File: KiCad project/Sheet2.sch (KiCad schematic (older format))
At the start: 7 parts, among them U1 EFM32GG332, X1 SMD_32.768kHz_CRYSTAL_OSC, X2 SMD_48MHZ_CRYSTAL_OSC

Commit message: IC packages, bugfixes
drawings for IC packages, associations, schematic fixes
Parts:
- U1: footprint (none) -> Housings_QFP:TQFP-64_10x10mm_Pitch0.5mm
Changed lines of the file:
@@
 $Descr A4 11693 8268
 encoding utf-8
-Sheet 3 7
+Sheet 3 10
 Title "uC part A"
 Date "14 March 2015"
@@
 F 0 "U1" H 7450 850 60  0000 C CNN
 F 1 "EFM32GG332" H 8850 850 60  0000 C CNN
-F 2 "" H 8850 850 60  0000 C CNN
+F 2 "Housings_QFP:TQFP-64_10x10mm_Pitch0.5mm" H 8850 850 60  0001 C CNN
 F 3 "" H 8850 850 60  0000 C CNN
 	1    7350 900
@@
 F 0 "X2" H 4900 3290 50  0000 C CNN
 F 1 "SMD_48MHZ_CRYSTAL_OSC" H 4930 3090 50  0000 L CNN
-F 2 "" H 4900 3200 60  0000 C CNN
+F 2 "" H 4900 3200 60  0001 C CNN
 F 3 "" H 4900 3200 60  0000 C CNN
 	1    4900 3200
@@
 F 0 "C17" H 4750 2950 50  0000 L CNN
 F 1 "C" H 4750 2750 50  0000 L CNN
-F 2 "" H 4738 2700 30  0000 C CNN
+F 2 "" H 4738 2700 30  0001 C CNN
 F 3 "" H 4700 2850 60  0000 C CNN
 	1    4700 2850
@@
 F 0 "C18" H 5150 2950 50  0000 L CNN
 F 1 "C" H 5150 2750 50  0000 L CNN
-F 2 "" H 5138 2700 30  0000 C CNN
+F 2 "" H 5138 2700 30  0001 C CNN
 F 3 "" H 5100 2850 60  0000 C CNN
 	1    5100 2850
@@
 	4700 3200 4700 3050
 $Comp
-L GND #PWR14
+L GND #PWR017
 U 1 1 5504D536
 P 4900 2500
-F 0 "#PWR14" H 4900 2250 60  0001 C CNN
+F 0 "#PWR017" H 4900 2250 60  0001 C CNN
 F 1 "GND" H 4900 2350 60  0000 C CNN
 F 2 "" H 4900 2500 60  0000 C CNN
@@
 F 0 "X1" H 5550 2590 50  0000 C CNN
 F 1 "SMD_32.768kHz_CRYSTAL_OSC" H 5580 2390 50  0000 L CNN
-F 2 "" H 5550 2500 60  0000 C CNN
+F 2 "" H 5550 2500 60  0001 C CNN
 F 3 "" H 5550 2500 60  0000 C CNN
 	1    5550 2500
@@
 F 0 "C16" H 5800 2250 50  0000 L CNN
 F 1 "C" H 5800 2050 50  0000 L CNN
-F 2 "" H 5788 2000 30  0000 C CNN
+F 2 "" H 5788 2000 30  0001 C CNN
 F 3 "" H 5750 2150 60  0000 C CNN
 	1    5750 2150
@@
 F 0 "C15" H 5400 2250 50  0000 L CNN
 F 1 "C" H 5400 2050 50  0000 L CNN
-F 2 "" H 5388 2000 30  0000 C CNN
+F 2 "" H 5388 2000 30  0001 C CNN
 F 3 "" H 5350 2150 60  0000 C CNN
 	1    5350 2150
@@
 Connection ~ 5350 2500
 $Comp
-L GND #PWR16
+L GND #PWR018
 U 1 1 5504D88A
 P 4900 3300
-F 0 "#PWR16" H 4900 3050 60  0001 C CNN
+F 0 "#PWR018" H 4900 3050 60  0001 C CNN
 F 1 "GND" H 4900 3150 60  0000 C CNN
 F 2 "" H 4900 3300 60  0000 C CNN
@@
 $EndComp
 $Comp
-L GND #PWR15
+L GND #PWR019
 U 1 1 5504D89E
 P 5550 2600
-F 0 "#PWR15" H 5550 2350 60  0001 C CNN
+F 0 "#PWR019" H 5550 2350 60  0001 C CNN
 F 1 "GND" H 5550 2450 60  0000 C CNN
 F 2 "" H 5550 2600 60  0000 C CNN

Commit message: New packages, PCB
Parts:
- removed X1: SMD_32.768kHz_CRYSTAL_OSC, symbol CRYSTAL_SMD
- added X1: 32.768kHz SMD Crystal, Anastasia:1.6x1.0CRYSTAL, symbol CRYSTAL
- C16: renamed from C15; footprint (none) -> Capacitors_SMD:C_0603
- C17: renamed from C16; footprint (none) -> Capacitors_SMD:C_0603
- C18: renamed from C17; footprint (none) -> Capacitors_SMD:C_0603
- C19: renamed from C18; footprint (none) -> Capacitors_SMD:C_0603
- X2: footprint (none) -> Anastasia:2x1.6
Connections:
- wire segments 25 -> 26
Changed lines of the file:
@@
 F 0 "X2" H 4900 3290 50  0000 C CNN
 F 1 "SMD_48MHZ_CRYSTAL_OSC" H 4930 3090 50  0000 L CNN
-F 2 "" H 4900 3200 60  0001 C CNN
+F 2 "Anastasia:2x1.6" H 4900 3200 60  0001 C CNN
 F 3 "" H 4900 3200 60  0000 C CNN
 	1    4900 3200
@@
 $EndComp
 $Comp
-L C C17
+L C C18
 U 1 1 5504D3F7
 P 4700 2850
-F 0 "C17" H 4750 2950 50  0000 L CNN
+F 0 "C18" H 4750 2950 50  0000 L CNN
 F 1 "C" H 4750 2750 50  0000 L CNN
-F 2 "" H 4738 2700 30  0001 C CNN
+F 2 "Capacitors_SMD:C_0603" H 4738 2700 30  0001 C CNN
 F 3 "" H 4700 2850 60  0000 C CNN
 	1    4700 2850
@@
 $EndComp
 $Comp
-L C C18
+L C C19
 U 1 1 5504D470
 P 5100 2850
-F 0 "C18" H 5150 2950 50  0000 L CNN
+F 0 "C19" H 5150 2950 50  0000 L CNN
 F 1 "C" H 5150 2750 50  0000 L CNN
-F 2 "" H 5138 2700 30  0001 C CNN
+F 2 "Capacitors_SMD:C_0603" H 5138 2700 30  0001 C CNN
 F 3 "" H 5100 2850 60  0000 C CNN
 	1    5100 2850
@@
 High Frequency \nCrystal Oscillator
 $Comp
-L CRYSTAL_SMD X1
-U 1 1 5504D70C
-P 5550 2500
-F 0 "X1" H 5550 2590 50  0000 C CNN
-F 1 "SMD_32.768kHz_CRYSTAL_OSC" H 5580 2390 50  0000 L CNN
-F 2 "" H 5550 2500 60  0001 C CNN
-F 3 "" H 5550 2500 60  0000 C CNN
-	1    5550 2500
-	1    0    0    -1
-$EndComp
-$Comp
-L C C16
+L C C17
 U 1 1 5504D74C
 P 5750 2150
-F 0 "C16" H 5800 2250 50  0000 L CNN
+F 0 "C17" H 5800 2250 50  0000 L CNN
 F 1 "C" H 5800 2050 50  0000 L CNN
-F 2 "" H 5788 2000 30  0001 C CNN
+F 2 "Capacitors_SMD:C_0603" H 5788 2000 30  0001 C CNN
 F 3 "" H 5750 2150 60  0000 C CNN
 	1    5750 2150
@@
 $EndComp
 $Comp
-L C C15
+L C C16
 U 1 1 5504D769
 P 5350 2150
-F 0 "C15" H 5400 2250 50  0000 L CNN
+F 0 "C16" H 5400 2250 50  0000 L CNN
 F 1 "C" H 5400 2050 50  0000 L CNN
-F 2 "" H 5388 2000 30  0001 C CNN
+F 2 "Capacitors_SMD:C_0603" H 5388 2000 30  0001 C CNN
 F 3 "" H 5350 2150 60  0000 C CNN
 	1    5350 2150
@@
 	1    0    0    -1
 $EndComp
+Text Notes 5950 2200 0    60   ~ 0
+Low Frequency\nReal-Time Clock \nCrystal Oscillator\n
 $Comp
-L GND #PWR019
-U 1 1 5504D89E
-P 5550 2600
-F 0 "#PWR019" H 5550 2350 60  0001 C CNN
-F 1 "GND" H 5550 2450 60  0000 C CNN
-F 2 "" H 5550 2600 60  0000 C CNN
-F 3 "" H 5550 2600 60  0000 C CNN
-	1    5550 2600
+L CRYSTAL X1
+U 1 1 550DBF8D
+P 5650 2700
+F 0 "X1" H 5650 2850 50  0000 C CNN
+F 1 "32.768kHz SMD Crystal" H 5650 2550 50  0000 C CNN
+F 2 "Anastasia:1.6x1.0CRYSTAL" H 5650 2700 60  0001 C CNN
+F 3 "" H 5650 2700 60  0000 C CNN
+	1    5650 2700
 	1    0    0    -1
 $EndComp
-Text Notes 5950 2200 0    60   ~ 0
-Low Frequency\nReal-Time Clock \nCrystal Oscillator\n
+Wire Wire Line
+	5950 2700 5950 2500
+Connection ~ 5950 2500
 $EndSCHEMATC

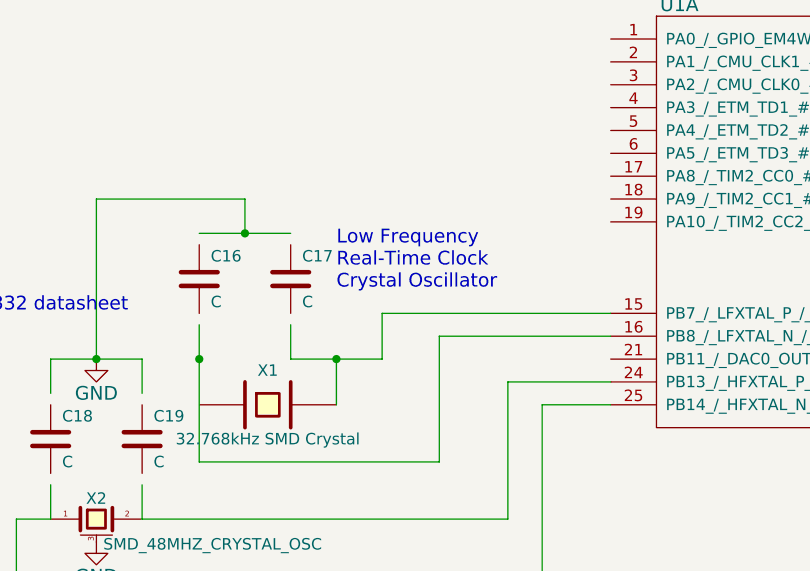
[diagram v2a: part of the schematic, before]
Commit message: Schematics, PCB design
New schematics for the pulse oximeter, PCB layout design
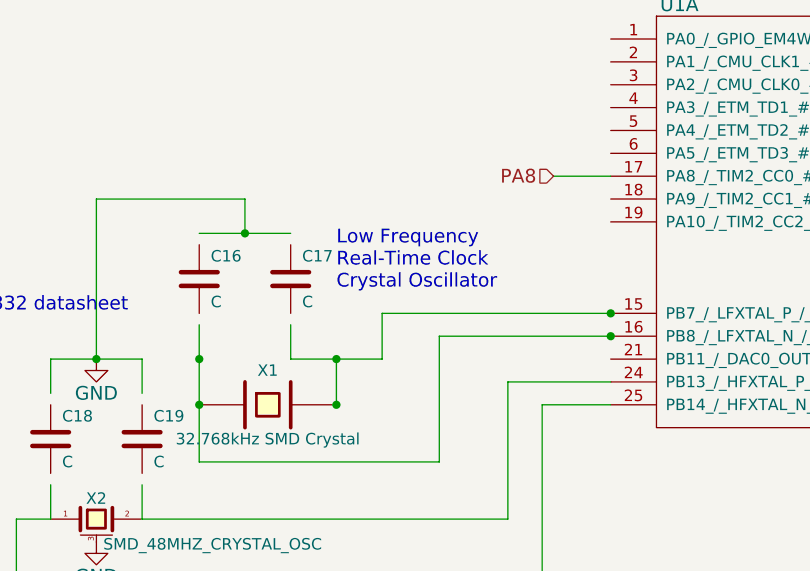
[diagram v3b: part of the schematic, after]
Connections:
- net labels added: PA8
- wire segments 26 -> 27
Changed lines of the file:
@@
 	5950 2700 5950 2500
 Connection ~ 5950 2500
+Connection ~ 5950 2700
+Connection ~ 5350 2700
+Connection ~ 7150 2400
+Connection ~ 7150 2300
+Text HLabel 6900 1700 0    60   Input ~ 0
+PA8
+Wire Wire Line
+	7150 1700 6900 1700
 $EndSCHEMATC

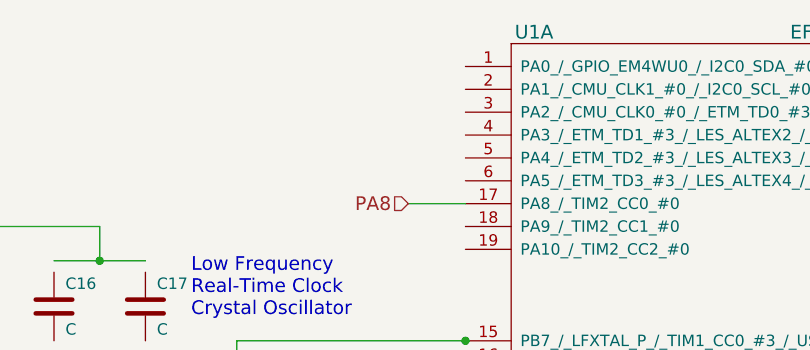
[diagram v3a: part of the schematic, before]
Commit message: PCB design
Routing for the main components, except for the power section
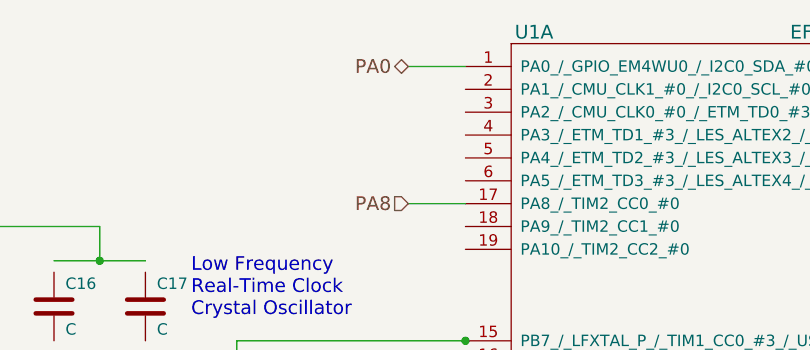
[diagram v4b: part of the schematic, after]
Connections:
- net labels added: PA0
- wire segments 27 -> 28
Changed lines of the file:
@@
 Wire Wire Line
 	7150 1700 6900 1700
+Text HLabel 6900 1100 0    60   3State ~ 0
+PA0
+Wire Wire Line
+	7150 1100 6900 1100
 $EndSCHEMATC

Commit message: PCB finalised, Gerbers created for v0.5
New footprints, fixes in schematic, PCB final design, plotted Gerbers
for prototype production
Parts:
- added SW4: SWITCH, Anastasia:KMS_SMD_SW, symbol SWITCH
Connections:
- net labels added: PA1, PA10, PA2, PA9
- wire segments 28 -> 34
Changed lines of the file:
@@
 $Descr A4 11693 8268
 encoding utf-8
-Sheet 3 10
+Sheet 2 10
 Title "uC part A"
 Date "14 March 2015"
@@
 	4700 3200 4700 3050
 $Comp
-L GND #PWR017
+L GND #PWR01
 U 1 1 5504D536
 P 4900 2500
-F 0 "#PWR017" H 4900 2250 60  0001 C CNN
+F 0 "#PWR01" H 4900 2250 60  0001 C CNN
 F 1 "GND" H 4900 2350 60  0000 C CNN
 F 2 "" H 4900 2500 60  0000 C CNN
@@
 Connection ~ 5350 2500
 $Comp
-L GND #PWR018
+L GND #PWR02
 U 1 1 5504D88A
 P 4900 3300
-F 0 "#PWR018" H 4900 3050 60  0001 C CNN
+F 0 "#PWR02" H 4900 3050 60  0001 C CNN
 F 1 "GND" H 4900 3150 60  0000 C CNN
 F 2 "" H 4900 3300 60  0000 C CNN
@@
 Wire Wire Line
 	7150 1100 6900 1100
+Text HLabel 6900 1200 0    60   3State ~ 0
+PA1
+Text HLabel 6900 1300 0    60   3State ~ 0
+PA2
+Wire Wire Line
+	7150 1200 6900 1200
+Wire Wire Line
+	6900 1300 7150 1300
+$Comp
+L GND #PWR03
+U 1 1 551928CE
+P 5350 1600
+F 0 "#PWR03" H 5350 1350 60  0001 C CNN
+F 1 "GND" H 5350 1450 60  0000 C CNN
+F 2 "" H 5350 1600 60  0000 C CNN
+F 3 "" H 5350 1600 60  0000 C CNN
+	1    5350 1600
+	1    0    0    -1
+$EndComp
+Wire Wire Line
+	6450 1600 7150 1600
+Text HLabel 6900 1800 0    60   3State ~ 0
+PA9
+Text HLabel 6900 1900 0    60   3State ~ 0
+PA10
+Wire Wire Line
+	6900 1800 7150 1800
+Wire Wire Line
+	6900 1900 7150 1900
+$Comp
+L SWITCH SW4
+U 1 1 55214730
+P 5950 1450
+F 0 "SW4" H 5950 1550 50  0000 C CNN
+F 1 "SWITCH" H 5950 1350 50  0000 C CNN
+F 2 "Anastasia:KMS_SMD_SW" H 5950 1450 60  0001 C CNN
+F 3 "" H 5950 1450 60  0000 C CNN
+	1    5950 1450
+	-1   0    0    -1
+$EndComp
+Wire Wire Line
+	5450 1600 5350 1600
 $EndSCHEMATC

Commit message: Refactoring
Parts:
- C16, C17: value C -> 15P
- C18, C19: value C -> 9P
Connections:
- wire segments 34 -> 36
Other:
- note removed: "Choose load capacitors\naccording to EFM32GG332 datasheet"
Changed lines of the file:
@@
 LIBS:memory
 LIBS:xilinx
-LIBS:special
 LIBS:microcontrollers
 LIBS:dsp
@@
 U 1 1 5504D3F7
 P 4700 2850
+AR Path="/5504D3F7" Ref="C18"  Part="1"
+AR Path="/5504D17E/5504D3F7" Ref="C18"  Part="1"
 F 0 "C18" H 4750 2950 50  0000 L CNN
-F 1 "C" H 4750 2750 50  0000 L CNN
+F 1 "9P" H 4750 2750 50  0000 L CNN
 F 2 "Capacitors_SMD:C_0603" H 4738 2700 30  0001 C CNN
 F 3 "" H 4700 2850 60  0000 C CNN
@@
 U 1 1 5504D470
 P 5100 2850
+AR Path="/5504D470" Ref="C19"  Part="1"
+AR Path="/5504D17E/5504D470" Ref="C19"  Part="1"
 F 0 "C19" H 5150 2950 50  0000 L CNN
-F 1 "C" H 5150 2750 50  0000 L CNN
+F 1 "9P" H 5150 2750 50  0000 L CNN
 F 2 "Capacitors_SMD:C_0603" H 5138 2700 30  0001 C CNN
 F 3 "" H 5100 2850 60  0000 C CNN
@@
 $EndComp
 Wire Wire Line
-	5100 3200 5100 3050
-Wire Wire Line
-	4700 3200 4700 3050
+	5100 3000 5100 3200
+Wire Wire Line
+	4700 3000 4700 3200
 $Comp
 L GND #PWR01
@@
 	4700 2500 5100 2500
 Wire Wire Line
-	5100 2500 5100 2650
-Wire Wire Line
-	4700 2500 4700 2650
+	5100 2500 5100 2700
+Wire Wire Line
+	4700 2500 4700 2700
 Connection ~ 4900 2500
 Wire Wire Line
@@
 Wire Wire Line
 	4550 3200 4550 3600
-Text Notes 3500 2300 0    60   ~ 0
-Choose load capacitors\naccording to EFM32GG332 datasheet
 Wire Wire Line
 	6700 3200 6700 2600
@@
 U 1 1 5504D74C
 P 5750 2150
+AR Path="/5504D74C" Ref="C17"  Part="1"
+AR Path="/5504D17E/5504D74C" Ref="C17"  Part="1"
 F 0 "C17" H 5800 2250 50  0000 L CNN
-F 1 "C" H 5800 2050 50  0000 L CNN
+F 1 "15P" H 5800 2050 50  0000 L CNN
 F 2 "Capacitors_SMD:C_0603" H 5788 2000 30  0001 C CNN
 F 3 "" H 5750 2150 60  0000 C CNN
@@
 U 1 1 5504D769
 P 5350 2150
+AR Path="/5504D769" Ref="C16"  Part="1"
+AR Path="/5504D17E/5504D769" Ref="C16"  Part="1"
 F 0 "C16" H 5400 2250 50  0000 L CNN
-F 1 "C" H 5400 2050 50  0000 L CNN
+F 1 "15P" H 5400 2050 50  0000 L CNN
 F 2 "Capacitors_SMD:C_0603" H 5388 2000 30  0001 C CNN
 F 3 "" H 5350 2150 60  0000 C CNN
@@
 Connection ~ 5550 1950
 Wire Wire Line
-	5350 2350 5350 2950
-Wire Wire Line
-	5750 2500 5750 2350
+	5350 2300 5350 2950
+Wire Wire Line
+	5750 2300 5750 2500
 Wire Wire Line
 	5750 2500 6150 2500
@@
 Wire Wire Line
 	5450 1600 5350 1600
+Wire Wire Line
+	5350 2000 5350 1950
+Wire Wire Line
+	5750 1950 5750 2000
 $EndSCHEMATC
